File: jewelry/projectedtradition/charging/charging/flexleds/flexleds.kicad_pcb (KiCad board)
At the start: 2 copper layers, 10 x 8 mm, 36 parts, among them J1 Conn_01x04, J2 Conn_01x04, J3 Conn_01x04, J4 Conn_01x04, J5 Conn_01x04, J6 Conn_01x04, J7 Conn_01x04

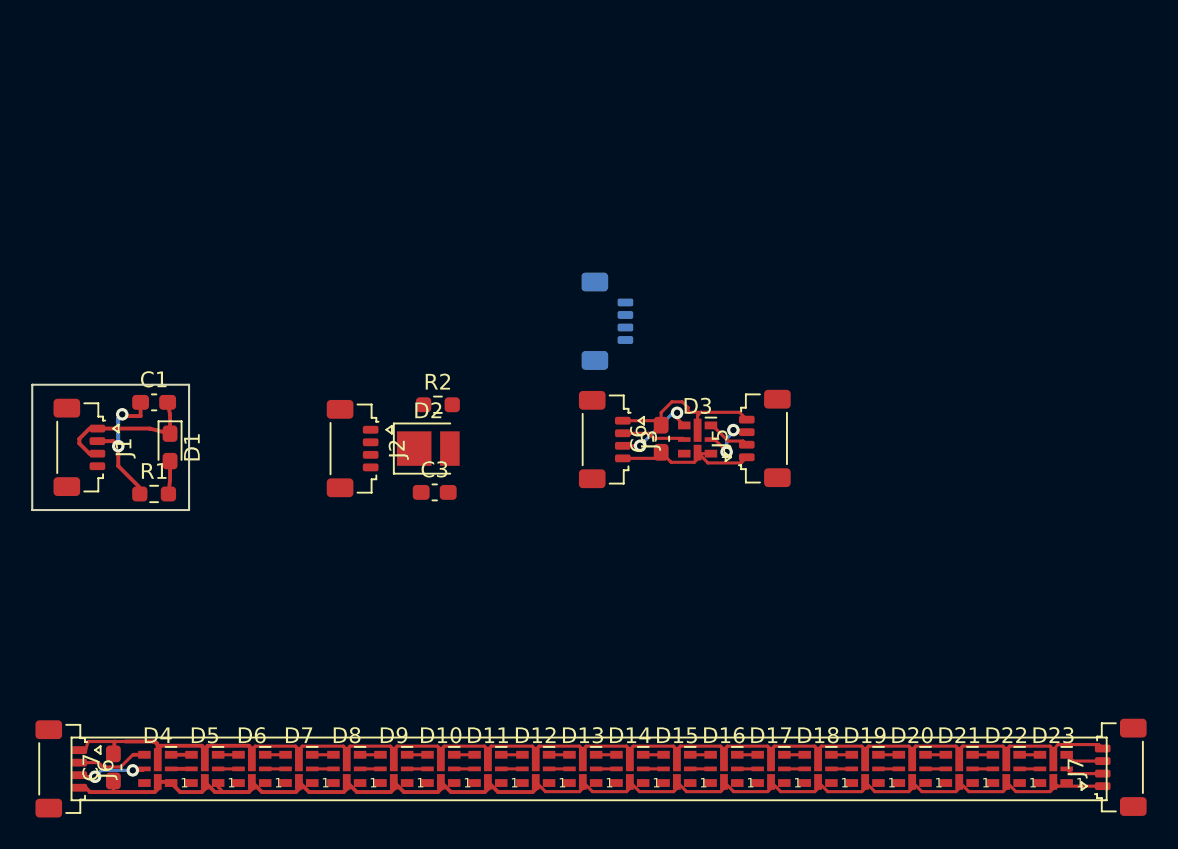
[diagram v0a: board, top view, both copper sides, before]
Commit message: jewelry: Flex leds almost ready
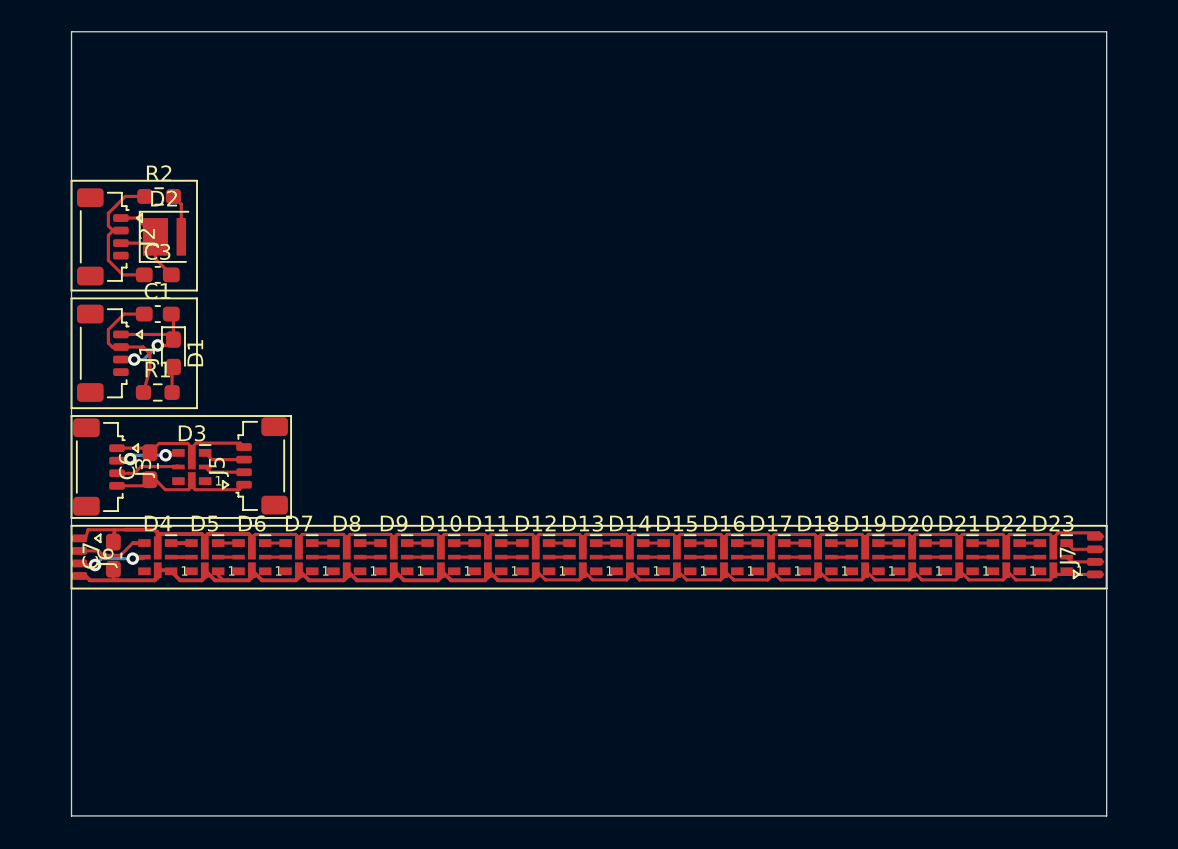
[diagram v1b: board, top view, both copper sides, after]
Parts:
- removed J4: Conn_01x04, Connector_JST:JST_SUR_SM04B-SURS-TF_1x04-1MP_P0.80mm_Horizontal
- D10, D11, D12, D13, D14, D15, D16, D17, D18, D19, D20, D21, D22, D23, D3, D4, D5, D6, D7, D8, D9: footprint LED_SMD:LED-APA102-2020 -> flexleds:LED-APA102-2020-midpower
- D2: footprint LED_SMD:LED_PLCC_2835 -> flexleds:LED_Cree-J3030
- J6, J7: footprint Connector_JST:JST_SUR_SM04B-SURS-TF_1x04-1MP_P0.80mm_Horizontal -> flexleds:JST_SUR_SM04B-SURS-TF_1x04-1MP_P0.80mm_Horizontal_cut
- moved C6 32.6 mm to (29.0, 38.2)
- moved D3 32.3 mm to (31.7, 38.2)
- moved J3 32.3 mm to (25.8, 38.2)
- moved J5 32.1 mm to (36.1, 38.2)
- moved C3 22.5 mm to (29.5, 26.0)
- moved R2 22.2 mm to (29.6, 21.0)
- moved D2 21.6 mm to (29.9, 23.6)
- moved J2 20.9 mm to (26.0, 23.6)
- moved J7 13.5 mm to (90.4, 43.9)
- moved C7 13.5 mm to (26.7, 43.9)
- moved D10 13.5 mm to (47.5, 44.0)
- moved D11 13.5 mm to (50.5, 44.0)
- moved D12 13.5 mm to (53.6, 44.0)
- moved D13 13.5 mm to (56.6, 44.0)
- moved D14 13.5 mm to (59.6, 44.0)
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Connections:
- net Net-(C1-Pad1) renamed /0603_led
- net Net-(C2-Pad1) renamed /0603_touch
- net Net-(C3-Pad1) renamed /3030_led
- net Net-(C4-Pad1) renamed /3030_touch
- C3 pad 2: Net-(C3-Pad2) -> GND
- C6 pad 2: Net-(C6-Pad2) -> GND
- D2 pad 1: Net-(C3-Pad2) -> GND
- D3 pad 6: Net-(C6-Pad2) -> GND
- J2 pad 1: Net-(C3-Pad2) -> GND
- J2 pad 3: Net-(C3-Pad2) -> GND
- J3 pad 1: Net-(C6-Pad2) -> GND
- J5 pad 4: Net-(C6-Pad2) -> GND
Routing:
- net GND: track 83.9 -> 101.2 mm
- net Net-(C6-Pad2): track 11.0 -> 0.00 mm
- net /3030_led: track 0.00 -> 9.19 mm
- net Net-(D2-Pad2): track 0.00 -> 2.78 mm
- net Net-(D3-Pad2): track 3.83 -> 2.62 mm, vias 2 -> 0
- net Net-(D3-Pad4): track 5.32 -> 4.13 mm
- net Net-(C6-Pad1): track 10.1 -> 9.34 mm
- net Net-(C1-Pad2): track 9.82 -> 9.04 mm, vias 0 -> 2
- net Net-(D1-Pad2): track 2.10 -> 1.54 mm
- net /0603_led: track 8.89 -> 9.01 mm, vias 2 -> 0
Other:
- board size 10 x 8 mm -> 66 x 50 mm

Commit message: jewelry: Flexleds layout complete and DRC clean
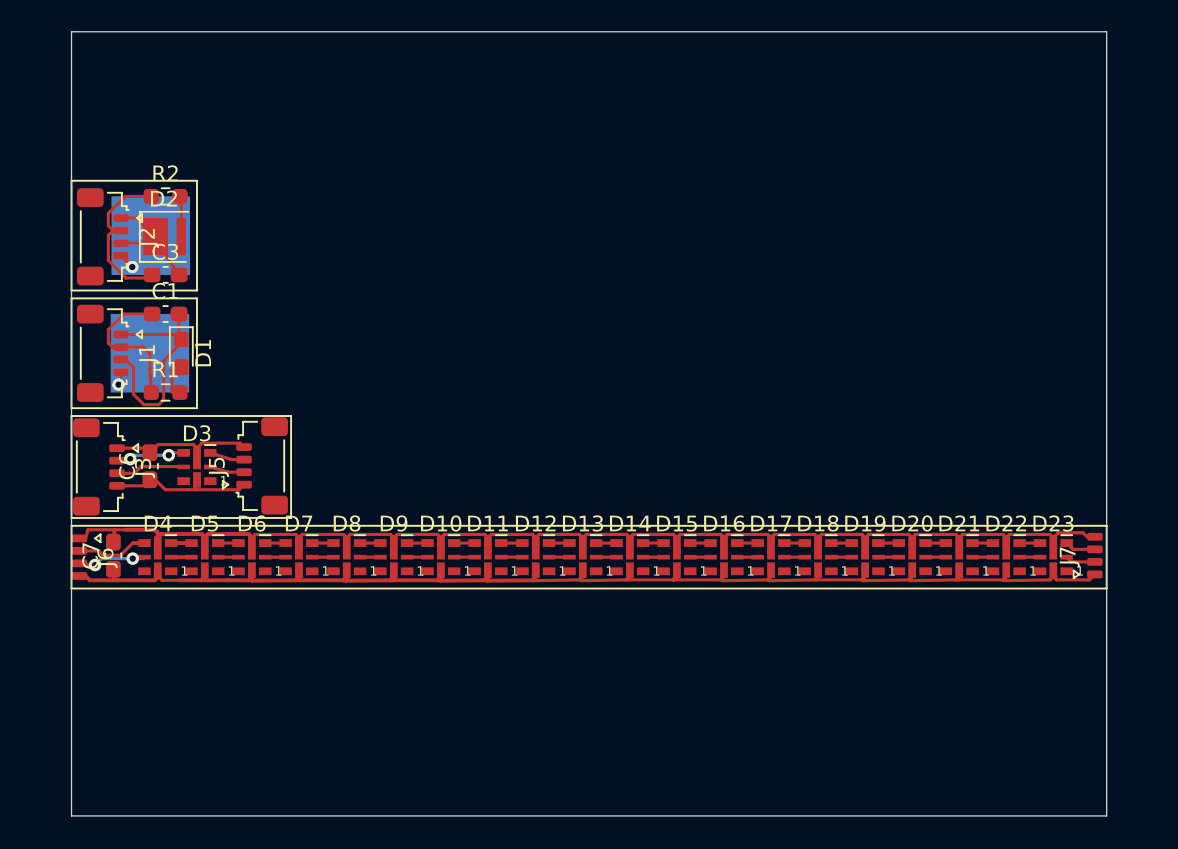
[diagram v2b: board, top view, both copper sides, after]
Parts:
- added J4: Conn_01x01, flexleds:touchpad, B.Cu at (28.9, 31.0)
- added J8: Conn_01x01, flexleds:touchpad, B.Cu at (29.0, 23.5)
- moved C1 0.50 mm to (30.0, 28.5)
- moved C3 0.50 mm to (30.0, 26.0)
- moved D1 0.50 mm to (31.0, 31.0)
- moved R1 0.50 mm to (30.0, 33.5)
- moved R2 0.41 mm to (30.0, 21.0)
- moved D3 0.33 mm to (32.0, 38.2)
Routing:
- net Net-(C7-Pad1): track 82.2 -> 90.2 mm
- net Net-(C1-Pad2): track 9.04 -> 15.2 mm, vias 2 -> 0
- net /3030_touch: track 0.00 -> 1.02 mm, vias 0 -> 1
- net /0603_touch: track 0.00 -> 0.86 mm, vias 0 -> 1
- net /3030_led: track 9.19 -> 9.86 mm
- net GND: track 101.2 -> 100.7 mm
- net Net-(D3-Pad3): track 2.76 -> 2.22 mm
- net Net-(D23-Pad3): track 2.47 -> 1.97 mm
- net Net-(D23-Pad2): track 2.42 -> 1.92 mm
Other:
- net class Default: clearance 0.2 -> 0.18
- rule trace_clearance: 0.2 -> 0.18

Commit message: jewelry: Flexleds silk clean
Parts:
- moved D3 15.0 mm to (32.0, 23.2)
- moved J3 15.0 mm to (25.8, 23.2)
- moved J5 15.0 mm to (36.1, 23.2)
- moved C6 15.0 mm to (29.0, 23.2)
- moved C1 7.00 mm to (30.0, 35.5)
- moved C3 7.00 mm to (30.0, 33.0)
- moved D1 7.00 mm to (31.0, 38.0)
- moved D2 7.00 mm to (29.9, 30.6)
- moved J1 7.00 mm to (26.0, 38.0)
- moved J2 7.00 mm to (26.0, 30.6)
- moved J4 7.00 mm to (28.9, 38.0)
- moved J8 7.00 mm to (29.0, 30.5)
- moved R1 7.00 mm to (30.0, 40.5)
- moved R2 7.00 mm to (30.0, 28.0)
